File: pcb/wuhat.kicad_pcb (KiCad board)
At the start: 2 copper layers, 65 x 30 mm, 44 parts, among them J1 GPIOcon, U1 MCP3002, U3 ID

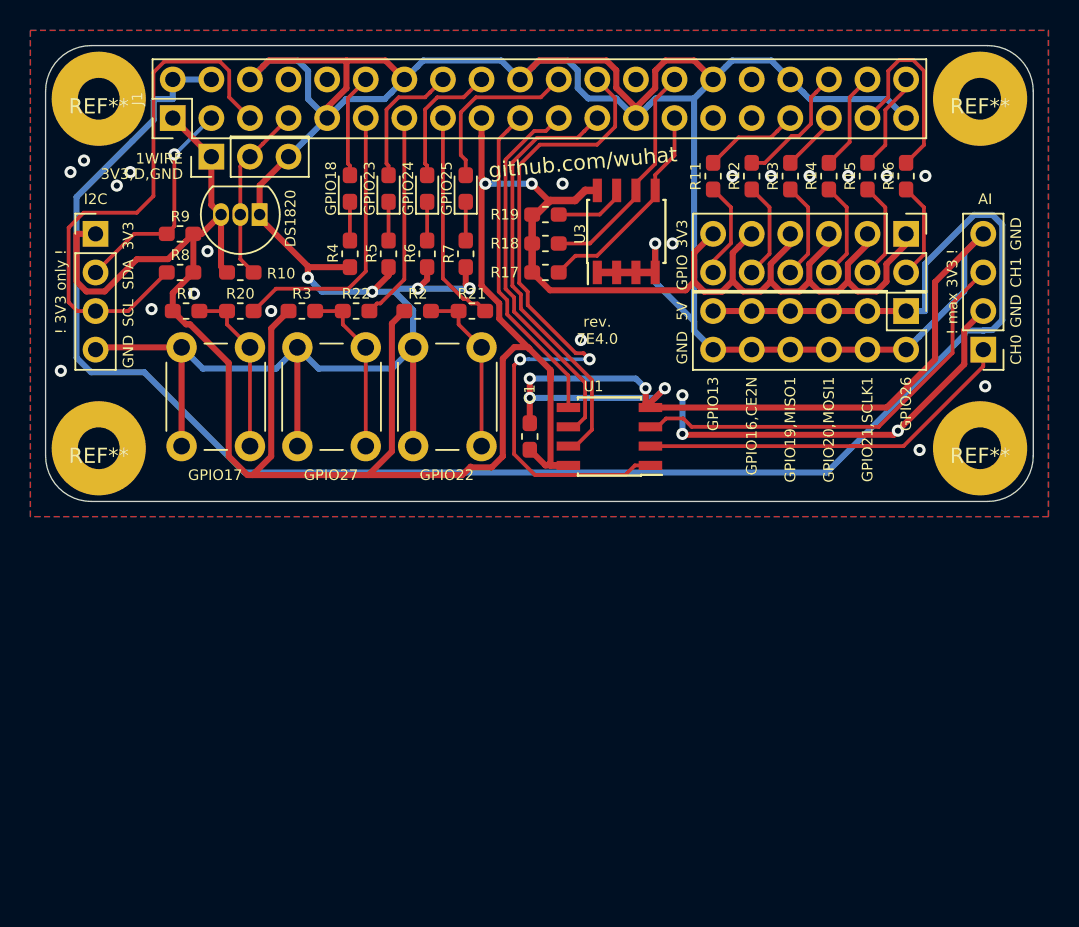
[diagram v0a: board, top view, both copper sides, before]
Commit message: moved mounting holes and board outline
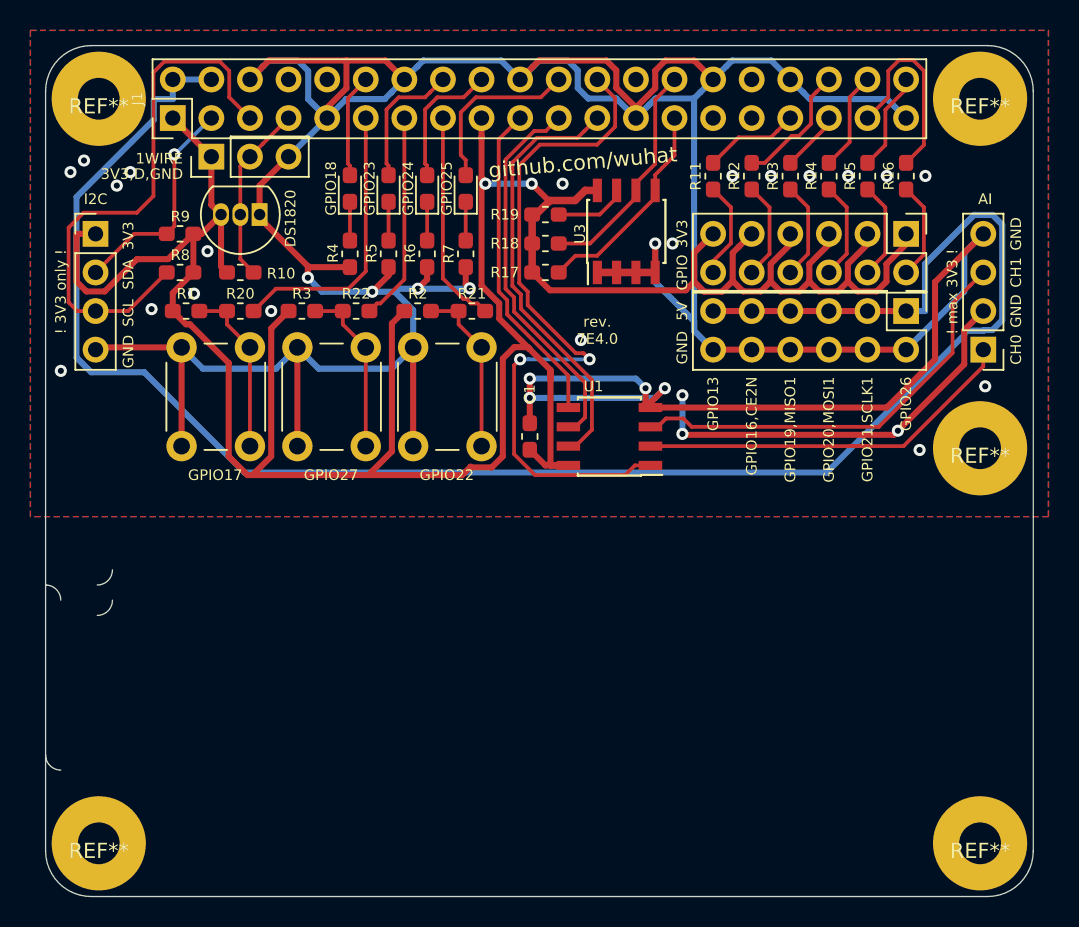
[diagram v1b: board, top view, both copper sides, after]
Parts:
- added REF**: mounting_hole, WUhat Artwork:mounting_hole, F.Cu at (163.1, 148.2)
- moved REF** 26.0 mm to (105.1, 148.2)
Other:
- board size 65 x 30 mm -> 65 x 56 mm
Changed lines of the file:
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@@
-(kicad_pcb (version 20171130) (host pcbnew "(5.1.4)-1")
+(kicad_pcb (version 20171130) (host pcbnew "(5.1.5)-2")
   (general
     (thickness 1.6)
-    (drawings 44)
+    (drawings 48)
     (tracks 509)
     (zones 0)
-    (modules 44)
+    (modules 45)
     (nets 42)
   )
@@
     (add_net GND)
   )
+  (module "WUhat Artwork:mounting_hole" (layer F.Cu)
+    (at 163.1 148.23)
+    (fp_text reference REF** (at 0 0.5) (layer F.SilkS)
+      (effects (font (size 1 1) (thickness 0.15)))
+    )
+    (fp_text value mounting_hole (at 0 -0.5) (layer F.Fab)
+      (effects (font (size 1 1) (thickness 0.15)))
+    )
+    (pad "" np_thru_hole circle (at 0 0) (size 6.2 6.2) (drill 2.75) (layers *.Cu *.Mask))
+  )
   (module "WUhat Artwork:qrcode" (layer B.Cu)
     (at 131.2425 114.724)
@@
   )
   (module "WUhat Artwork:mounting_hole" (layer F.Cu)
-    (at 105.1 122.23)
+    (at 105.1 148.23)
     (fp_text reference REF** (at 0 0.5) (layer F.SilkS)
       (effects (font (size 1 1) (thickness 0.15)))
@@
     (pad "" np_thru_hole circle (at 0 0) (size 6.2 6.2) (drill 2.75) (layers *.Cu *.Mask))
   )
+  (gr_arc (start 101.6 132.23) (end 102.6 132.23) (angle -90) (layer Edge.Cuts) (width 0.001))
+  (gr_arc (start 102.6 142.41) (end 101.6 142.41) (angle -90) (layer Edge.Cuts) (width 0.001))
+  (gr_arc (start 105 130.23) (end 105 131.23) (angle -90) (layer Edge.Cuts) (width 0.001))
+  (gr_arc (start 105 132.23) (end 105 133.23) (angle -90) (layer Edge.Cuts) (width 0.001))
   (gr_text "rev.\n7E4.0" (at 137.91 114.47) (layer F.SilkS)
     (effects (font (size 0.7 0.7) (thickness 0.15)))
@@
   (gr_line (start 108.7 96.69) (end 108.7 101.77) (layer Cmts.User) (width 0.001))
   (gr_line (start 134.1 102.23) (end 134.1 96.73) (layer Cmts.User) (width 0.15))
-  (gr_line (start 166.6 122.73) (end 166.6 98.73) (layer Edge.Cuts) (width 0.001))
-  (gr_arc (start 163.6 122.73) (end 163.6 125.73) (angle -90) (layer Edge.Cuts) (width 0.001))
-  (gr_line (start 104.6 125.73) (end 163.6 125.73) (layer Edge.Cuts) (width 0.001))
+  (gr_line (start 166.6 148.73) (end 166.6 98.73) (layer Edge.Cuts) (width 0.001))
+  (gr_arc (start 163.6 148.73) (end 163.6 151.73) (angle -90) (layer Edge.Cuts) (width 0.001))
+  (gr_line (start 104.6 151.73) (end 163.6 151.73) (layer Edge.Cuts) (width 0.001))
   (gr_circle (center 163.1 122.23) (end 164.475 122.23) (layer Dwgs.User) (width 0.001))
   (gr_circle (center 105.1 122.23) (end 106.475 122.23) (layer Dwgs.User) (width 0.001))
   (gr_circle (center 163.1 99.23) (end 164.475 99.23) (layer Dwgs.User) (width 0.001))
   (gr_circle (center 105.1 99.23) (end 106.475 99.23) (layer Dwgs.User) (width 0.001))
-  (gr_arc (start 104.6 122.73) (end 101.6 122.73) (angle -90) (layer Edge.Cuts) (width 0.001))
-  (gr_line (start 101.6 98.73) (end 101.6 122.73) (layer Edge.Cuts) (width 0.001))
+  (gr_arc (start 104.6 148.73) (end 101.6 148.73) (angle -90) (layer Edge.Cuts) (width 0.001))
+  (gr_line (start 101.6 98.73) (end 101.6 148.73) (layer Edge.Cuts) (width 0.001))
   (gr_arc (start 104.6 98.73) (end 104.6 95.73) (angle -90) (layer Edge.Cuts) (width 0.001))
   (gr_line (start 163.6 95.73) (end 104.6 95.73) (layer Edge.Cuts) (width 0.001))

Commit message: notch added
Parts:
- moved I2C1 2.54 mm to (104.9, 105.6)
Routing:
- net /SCL: track 36.4 -> 33.6 mm
- net +5V: track 122.5 -> 124.0 mm
- net GND: track 301.7 -> 302.7 mm
- net /SDA: track 14.6 -> 13.5 mm
- net +3V3: track 190.0 -> 188.9 mm
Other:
- outline, holes or cut-outs redrawn
- board text added: "rev. 7E4.1"
- board text removed: "rev. 7E4.0"
